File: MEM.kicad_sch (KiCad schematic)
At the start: 12 parts, among them J6 Conn_01x01_Socket, J7 Conn_01x01_Socket, J8 Conn_01x01_Socket, J9 Conn_01x01_Socket, U3 SST39SF040, U4 SST39SF040, U5 AS6C4008-55PCN, U6 AS6C4008-55PCN

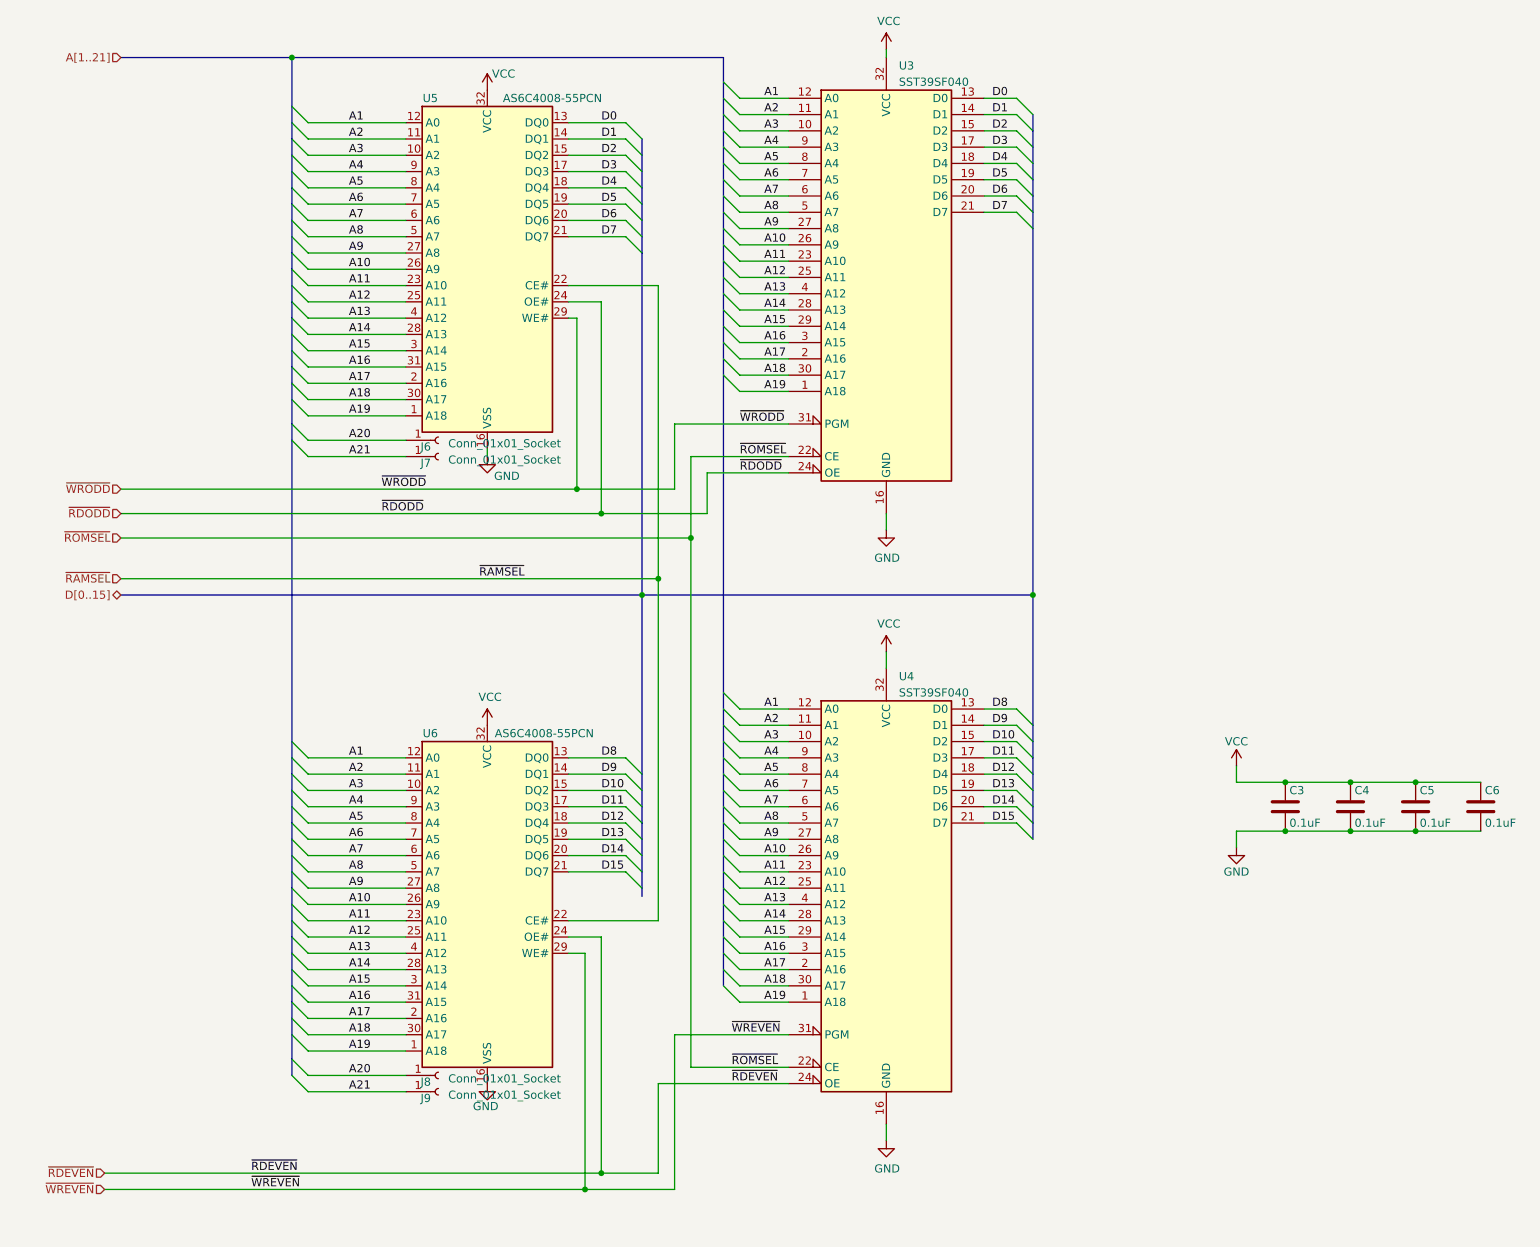
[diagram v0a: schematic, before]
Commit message: V1C version of BITSY that uses an SRAM SIMM for memory.
This version sent to JLCPCB on 08/15/2025.
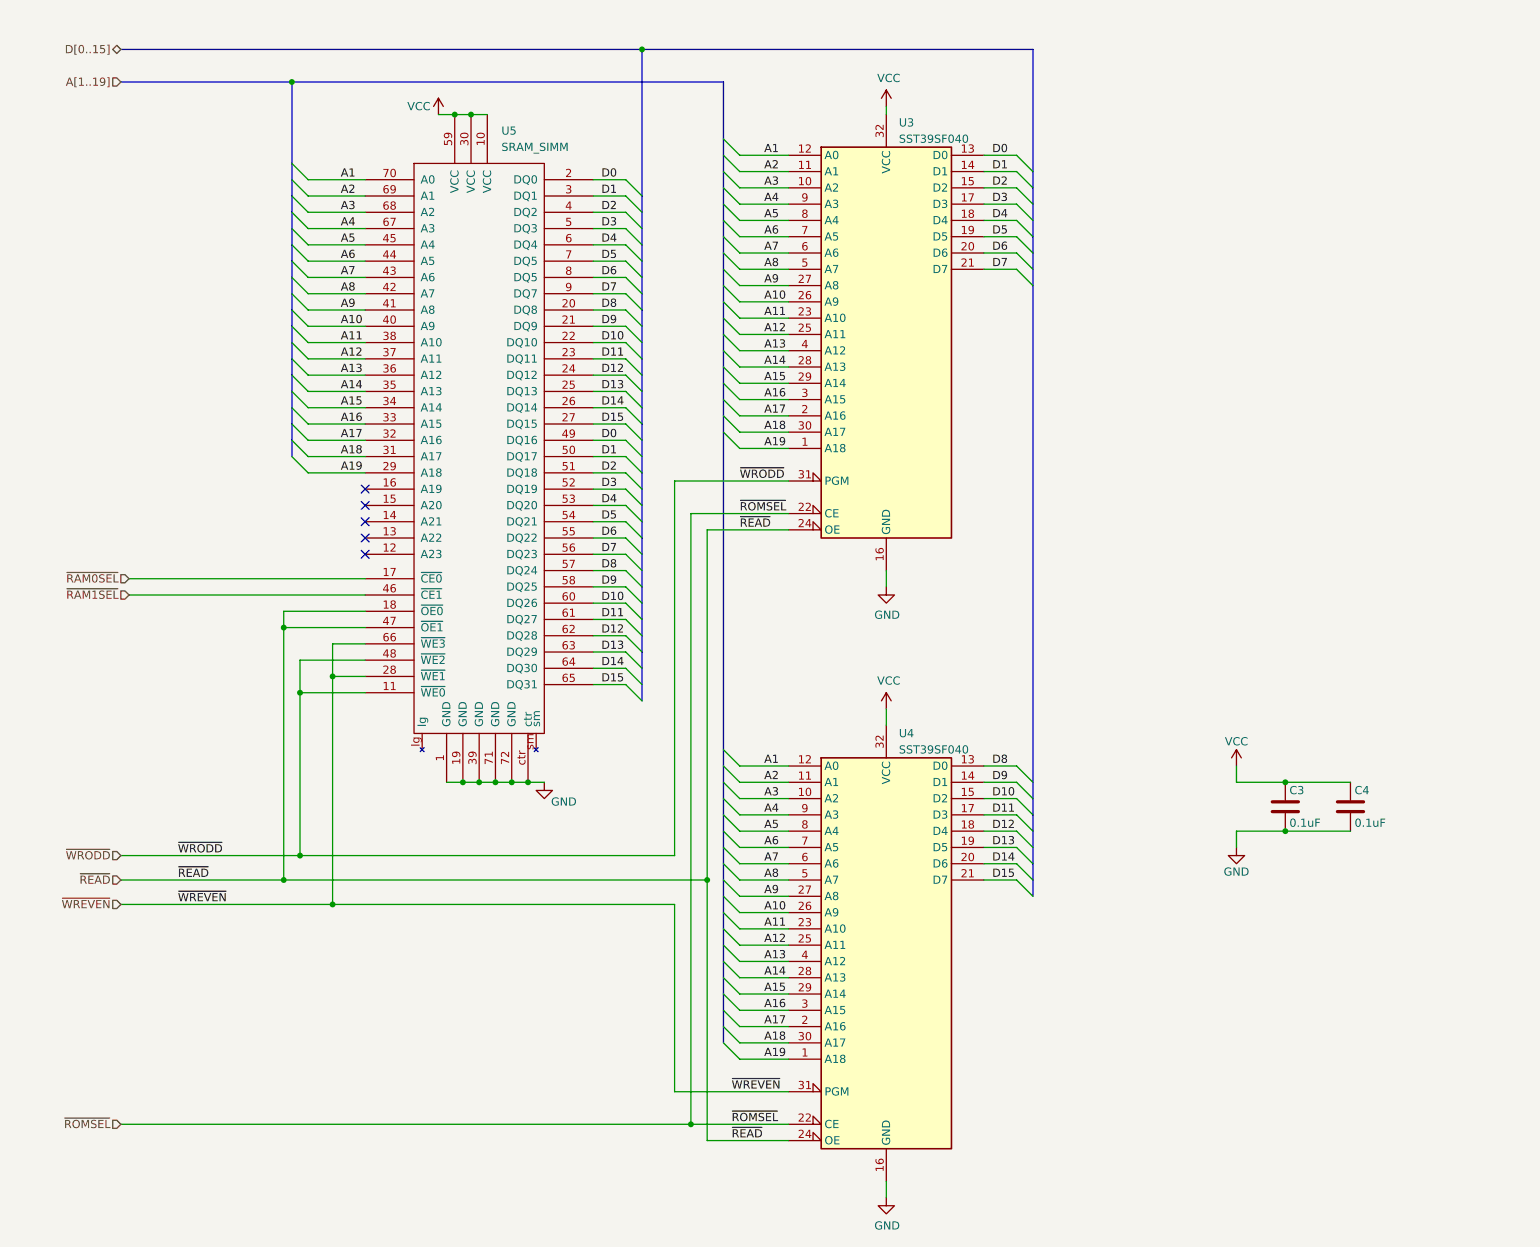
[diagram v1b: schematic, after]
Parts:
- removed C5, C6: 0.1uF, Capacitor_THT:C_Rect_L7.0mm_W2.0mm_P5.00mm, symbol Device:C
- removed J6, J7, J8, J9: Conn_01x01_Socket, Connector_PinSocket_2.54mm:PinSocket_1x01_P2.54mm_Vertical, symbol Connector:Conn_01x01_Socket
- removed U5, U6: AS6C4008-55PCN, Package_DIP:DIP-32_W15.24mm, symbol Memory_RAM:AS6C4008-55PCN
- added U5: SRAM_SIMM, SRAM_SIMM:DRAM-72-2021, symbol SRAM_SIMM:SRAM_SIMM
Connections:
- net ~{RDODD} is gone; now on net ~{READ}: U3.24 (OE)
- net A1: now also U5.70 (A0)
- net A10: now also U5.40 (A9)
- net A11: now also U5.38 (A10)
- net A12: now also U5.37 (A11)
- net A13: now also U5.36 (A12)
- net A14: now also U5.35 (A13)
- net A15: now also U5.34 (A14)
- net A16: now also U5.33 (A15)
- net A17: now also U5.32 (A16)
- net A18: now also U5.31 (A17)
- net A19: now also U5.29 (A18)
- net A2: now also U5.69 (A1)
- net A3: now also U5.68 (A2)
- net A4: now also U5.67 (A3)
- net A5: now also U5.45 (A4)
- net A6: now also U5.44 (A5)
- net A7: now also U5.43 (A6)
- net A8: now also U5.42 (A7)
- net A9: now also U5.41 (A8)
- net D0: now also U5.2 (DQ0), U5.49 (DQ16)
- net D1: now also U5.3 (DQ1), U5.50 (DQ17)
- net D10: now also U5.22 (DQ10), U5.60 (DQ26)
- net D11: now also U5.23 (DQ11), U5.61 (DQ27)
- net D12: now also U5.24 (DQ12), U5.62 (DQ28)
- net D13: now also U5.25 (DQ13), U5.63 (DQ29)
- net D14: now also U5.26 (DQ14), U5.64 (DQ30)
- net D15: now also U5.27 (DQ15), U5.65 (DQ31)
- net D2: now also U5.4 (DQ2), U5.51 (DQ18)
- net D3: now also U5.5 (DQ3), U5.52 (DQ19)
- net D4: now also U5.53 (DQ20), U5.6 (DQ4)
- net D5: now also U5.54 (DQ21), U5.7 (DQ5)
- net D6: now also U5.55 (DQ22), U5.8 (DQ5)
- net D7: now also U5.56 (DQ23), U5.9 (DQ7)
- net D8: now also U5.20 (DQ8), U5.57 (DQ24)
- net D9: now also U5.21 (DQ9), U5.58 (DQ25)
- net GND: now also U5.1 (GND), U5.19 (GND), U5.39 (GND), U5.71 (GND), U5.72 (GND), U5.ctr
- net VCC: now also U5.10 (VCC), U5.30 (VCC), U5.59 (VCC)
- net ~{WREVEN}: now also U5.28 (~{WE1}), U5.66 (~{WE3})
- net ~{WRODD}: now also U5.11 (~{WE0}), U5.48 (~{WE2})
- net ~{RDEVEN} renamed ~{READ}
- net ~{READ}: now also U5.18 (~{OE0}), U5.47 (~{OE1})
- new net ~{RAM0SEL}: U5.17 (~{CE0})
- new net ~{RAM1SEL}: U5.46 (~{CE1})
- no-connect marks 0 -> 5
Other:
- moved on the sheet: U3, U4

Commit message: Add part numbers.
No board change.
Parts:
- U5: PartNum00 (none) -> 571-5822021-4; PartVendor00 (none) -> Mouser
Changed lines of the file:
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@@
 			)
 		)
-		(property "Description" ""
+		(property "Description" "SIMM Connectors 72 POS SIMM VERT TIN"
 			(at 81.28 81.28 0)
 			(effects
+				(font
+					(size 1.27 1.27)
+				)
+				(hide yes)
+			)
+		)
+		(property "PartNum00" "571-5822021-4"
+			(at 81.28 81.28 0)
+			(effects
+				(font
+					(size 1.27 1.27)
+				)
+				(hide yes)
+			)
+		)
+		(property "PartVendor00" "Mouser"
+			(at 81.28 81.28 0)
+			(effects

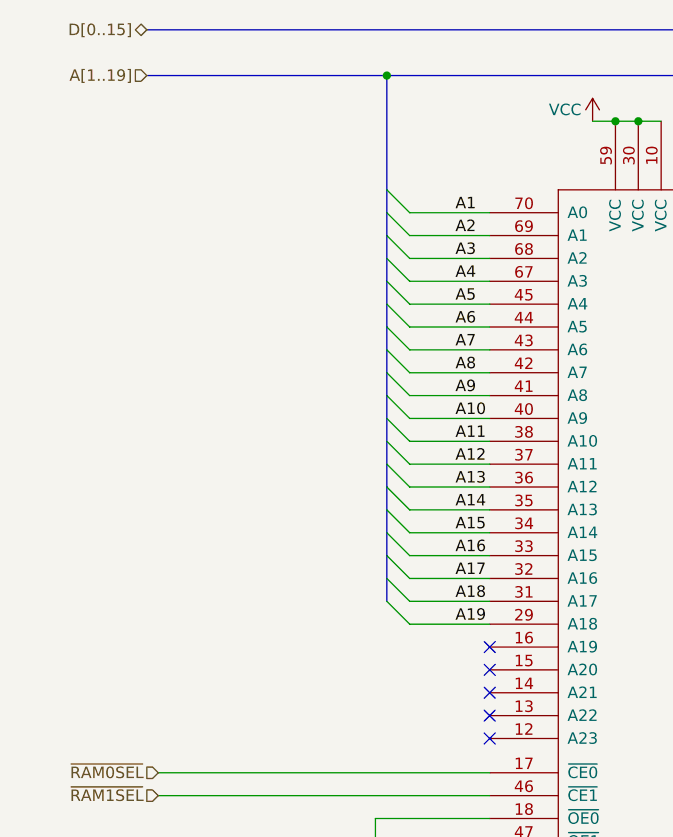
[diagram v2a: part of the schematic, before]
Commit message: Add two extra SIMM address lines.
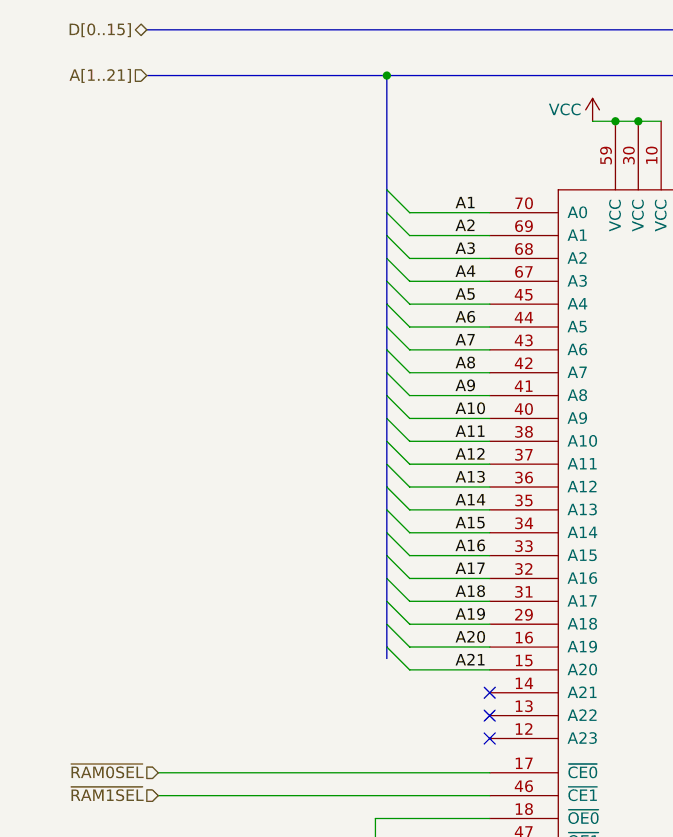
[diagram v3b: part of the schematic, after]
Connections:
- net A21: now reaches U5.15 (A20)
- net A20: now reaches U5.16 (A19)
- no-connect marks 5 -> 3
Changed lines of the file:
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@@
 	)
 	(no_connect
-		(at 63.5 87.63)
-	)
-	(no_connect
 		(at 63.5 97.79)
 	)
 	(no_connect
-		(at 63.5 90.17)
-	)
-	(no_connect
 		(at 63.5 95.25)
 	)
@@
 	)
 	(bus_entry
+		(at 52.07 85.09)
+		(size 2.54 2.54)
+		(stroke
+			(width 0)
+			(type default)
+		)
+	)
+	(bus_entry
 		(at 104.14 110.49)
 		(size 2.54 2.54)
@@
 	)
 	(bus_entry
+		(at 52.07 87.63)
+		(size 2.54 2.54)
+		(stroke
+			(width 0)
+			(type default)
+		)
+	)
+	(bus_entry
 		(at 104.14 44.45)
 		(size 2.54 2.54)
@@
 		)
 	)
+	(bus
+		(pts
+			(xy 52.07 87.63) (xy 52.07 88.9)
+		)
+		(stroke
+			(width 0)
+			(type default)
+		)
+	)
 	(wire
 		(pts
@@
 		)
 	)
+	(wire
+		(pts
+			(xy 54.61 90.17) (xy 63.5 90.17)
+		)
+		(stroke
+			(width 0)
+			(type default)
+		)
+	)
 	(bus
 		(pts
@@
 		)
 	)
+	(bus
+		(pts
+			(xy 52.07 85.09) (xy 52.07 87.63)
+		)
+		(stroke
+			(width 0)
+			(type default)
+		)
+	)
 	(wire
 		(pts
@@
 		)
 	)
+	(bus
+		(pts
+			(xy 52.07 82.55) (xy 52.07 85.09)
+		)
+		(stroke
+			(width 0)
+			(type default)
+		)
+	)
 	(wire
 		(pts
@@
 		)
 	)
+	(wire
+		(pts
+			(xy 54.61 87.63) (xy 63.5 87.63)
+		)
+		(stroke
+			(width 0)
+			(type default)
+		)
+	)
 	(bus
 		(pts
@@
 		)
 	)
+	(label "A21"
+		(at 59.69 90.17 0)
+		(effects
+			(font
+				(size 1.27 1.27)
+			)
+			(justify left bottom)
+		)
+	)
 	(label "D11"
 		(at 100.33 67.31 0)
@@
 		)
 	)
+	(label "A20"
+		(at 59.69 87.63 0)
+		(effects
+			(font
+				(size 1.27 1.27)
+			)
+			(justify left bottom)
+		)
+	)
 	(label "D5"
 		(at 100.33 52.07 0)
@@
 		)
 	)
-	(hierarchical_label "A[1..19]"
+	(hierarchical_label "A[1..21]"
 		(shape input)
 		(at 25.4 24.13 180)

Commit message: Update part numbers.
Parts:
- U3, U4: PartNum01 575-943224 -> 649-54020-32030LF
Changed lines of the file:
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@@
 			)
 		)
-		(property "PartNum01" "575-943224"
+		(property "PartNum01" "649-54020-32030LF"
 			(at 144.78 161.29 0)
 			(effects
@@
 			)
 		)
-		(property "PartNum01" "575-943224"
+		(property "PartNum01" "649-54020-32030LF"
 			(at 144.78 66.04 0)
 			(effects

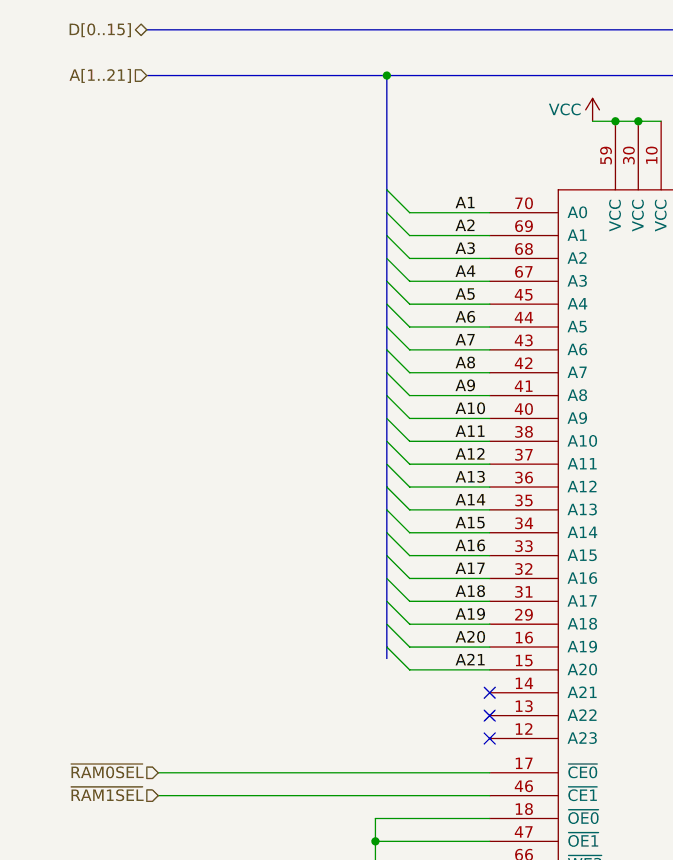
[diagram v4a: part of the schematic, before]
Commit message: Create V1E version.
Adds extra address line to SIMM for 16 MB support.
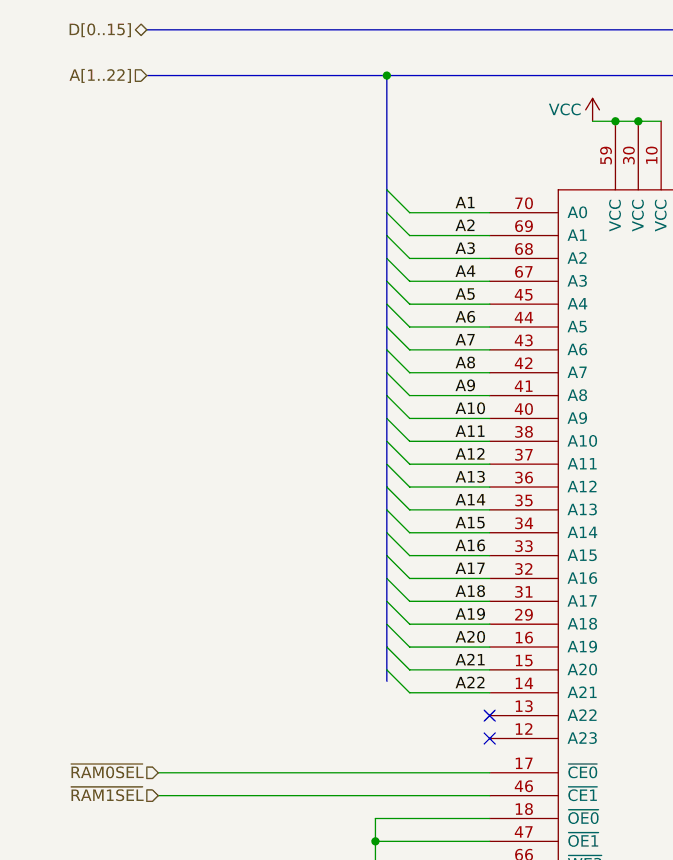
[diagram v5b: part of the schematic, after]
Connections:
- net A22: now reaches U5.14 (A21)
- no-connect marks 3 -> 2
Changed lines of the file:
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@@
 	(title_block
 		(title "BITSY Mark I - An MC68000 Single Board Computer")
-		(date "2025-08-15")
-		(rev "V1C")
+		(date "2025-11-09")
+		(rev "V1E")
 		(comment 1 "Licensed under CC-BY-SA-NC 4.0.")
 		(comment 2 "https://github.com/codesmythe/BITSY_MK_I")
@@
 		(at 63.5 95.25)
 	)
-	(no_connect
-		(at 63.5 92.71)
-	)
 	(bus_entry
 		(at 119.38 66.04)
@@
 	)
 	(bus_entry
+		(at 52.07 90.17)
+		(size 2.54 2.54)
+		(stroke
+			(width 0)
+			(type default)
+		)
+	)
+	(bus_entry
 		(at 119.38 148.59)
 		(size 2.54 2.54)
@@
 	(bus
 		(pts
-			(xy 52.07 87.63) (xy 52.07 88.9)
+			(xy 52.07 87.63) (xy 52.07 90.17)
 		)
 		(stroke
@@
 	(wire
 		(pts
+			(xy 54.61 92.71) (xy 63.5 92.71)
+		)
+		(stroke
+			(width 0)
+			(type default)
+		)
+	)
+	(wire
+		(pts
 			(xy 121.92 156.21) (xy 129.54 156.21)
 		)
@@
 		)
 	)
+	(bus
+		(pts
+			(xy 52.07 90.17) (xy 52.07 91.44)
+		)
+		(stroke
+			(width 0)
+			(type default)
+		)
+	)
 	(wire
 		(pts
@@
 		)
 	)
+	(label "A22"
+		(at 59.69 92.71 0)
+		(effects
+			(font
+				(size 1.27 1.27)
+			)
+			(justify left bottom)
+		)
+	)
 	(label "~{WREVEN}"
 		(at 34.29 152.4 0)
@@
 		)
 	)
-	(hierarchical_label "A[1..21]"
+	(hierarchical_label "A[1..22]"
 		(shape input)
 		(at 25.4 24.13 180)
